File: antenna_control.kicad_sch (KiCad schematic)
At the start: 26 parts, among them J7 G125-MH11005L1P, J9 FTSH-105-01-L-DV-K, Q13 DMP3056LDM-7, U46 M0L1228QRGERQ1, U59 TPS22919DCK

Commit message: Change all instances of K (for kilo) to k
That's the standard.

Signed-off-by: Corey Minyard <corey@minyard.net>
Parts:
- R136, R137, R177, R178: value 10KΩ -> 10kΩ
- R147, R151, R152, R153, R166, R167: value 2.2KΩ -> 2.2kΩ
- R195: value 4.7KΩ -> 4.7kΩ
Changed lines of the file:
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@@
 			)
 		)
-		(property "Value" "2.2KΩ"
+		(property "Value" "2.2kΩ"
 			(at 255.778 120.396 0)
 			(show_name no)
@@
 			)
 		)
-		(property "Value" "10KΩ"
+		(property "Value" "10kΩ"
 			(at 231.648 74.676 0)
 			(show_name no)
@@
 			)
 		)
-		(property "Value" "2.2KΩ"
+		(property "Value" "2.2kΩ"
 			(at 144.018 176.276 0)
 			(show_name no)
@@
 			)
 		)
-		(property "Value" "10KΩ"
+		(property "Value" "10kΩ"
 			(at 65.278 79.756 0)
 			(show_name no)
@@
 			)
 		)
-		(property "Value" "10KΩ"
+		(property "Value" "10kΩ"
 			(at 43.942 26.924 0)
 			(show_name no)
@@
 			)
 		)
-		(property "Value" "2.2KΩ"
+		(property "Value" "2.2kΩ"
 			(at 255.778 148.336 0)
 			(show_name no)
@@
 			)
 		)
-		(property "Value" "4.7KΩ"
+		(property "Value" "4.7kΩ"
 			(at 132.334 45.466 90)
 			(show_name no)
@@
 			)
 		)
-		(property "Value" "10KΩ"
+		(property "Value" "10kΩ"
 			(at 35.052 26.924 0)
 			(show_name no)
@@
 			)
 		)
-		(property "Value" "2.2KΩ"
+		(property "Value" "2.2kΩ"
 			(at 245.618 120.396 0)
 			(show_name no)
@@
 			)
 		)
-		(property "Value" "2.2KΩ"
+		(property "Value" "2.2kΩ"
 			(at 245.618 148.336 0)
 			(show_name no)
@@
 			)
 		)
-		(property "Value" "2.2KΩ"
+		(property "Value" "2.2kΩ"
 			(at 152.908 176.276 0)
 			(show_name no)

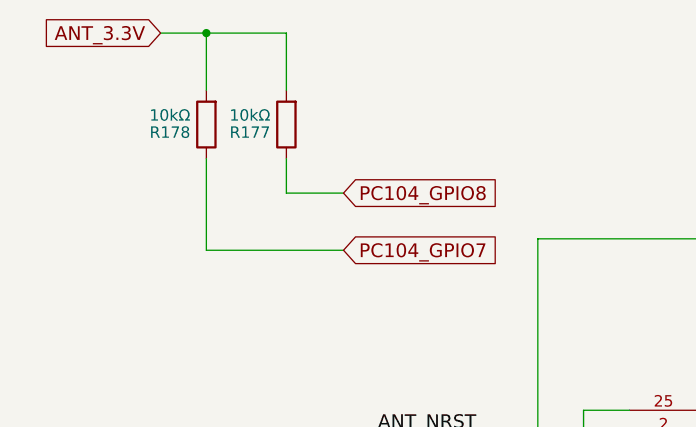
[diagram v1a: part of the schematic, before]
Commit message: Remove the extra power feeds on the 47-52 pins of the PC104 J1
They aren't needed.

Signed-off-by: Corey Minyard <corey@minyard.net>
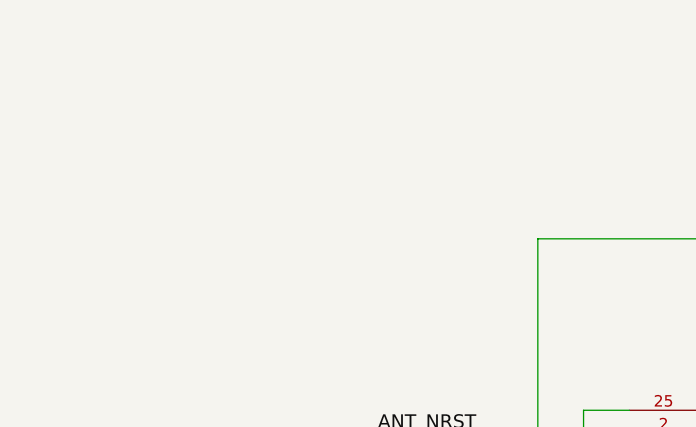
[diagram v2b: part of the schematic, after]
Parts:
- removed R177, R178: 10kΩ, Resistor_SMD:R_0402_1005Metric_Pad0.72x0.64mm_HandSolder, symbol Device:R

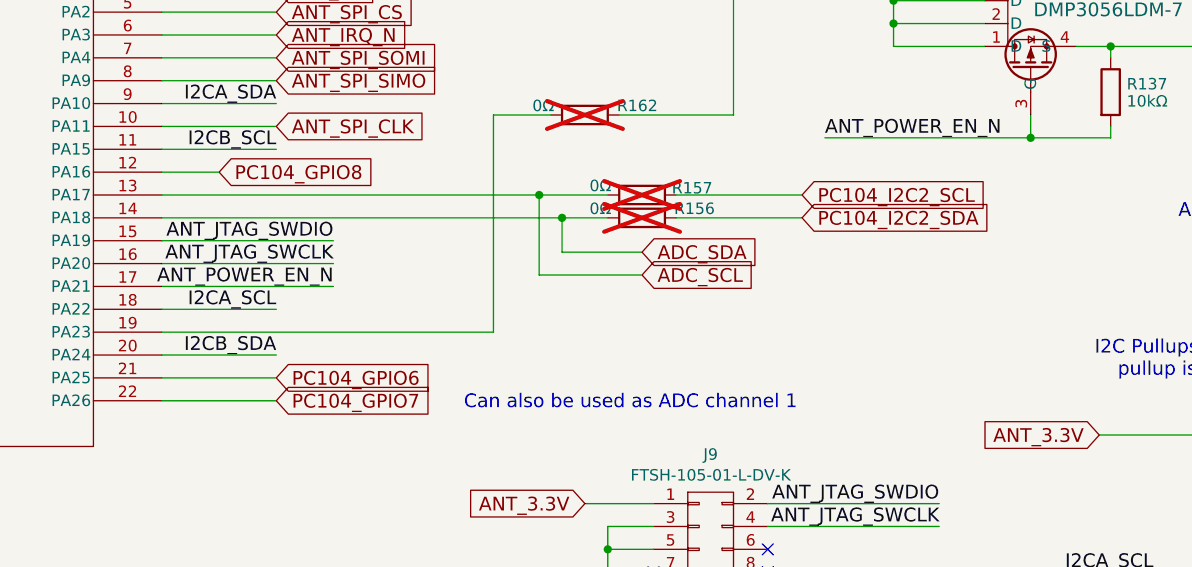
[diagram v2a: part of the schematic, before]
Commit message: Latch up protect all the PC104 lines
Add TMUX2821s to all the lines that need it.

Remove the ADC lines from the PC104.  I don't see any need for them and
I've never seen them on other boards.

Signed-off-by: Corey Minyard <corey@minyard.net>
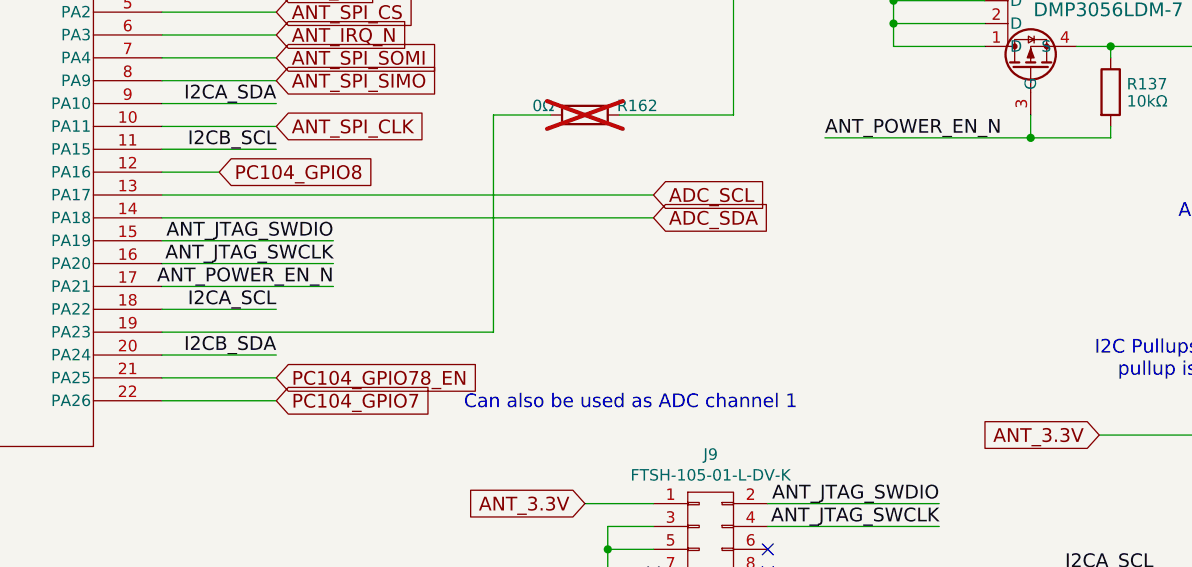
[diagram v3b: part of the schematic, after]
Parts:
- removed R156, R157: 0Ω, Resistor_SMD:R_0402_1005Metric_Pad0.72x0.64mm_HandSolder, symbol Device:R
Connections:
- net PC104_GPIO6 renamed PC104_GPIO78_EN
